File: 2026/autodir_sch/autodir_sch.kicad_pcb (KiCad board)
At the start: 2 copper layers, 34.5 x 16 mm, 12 parts, among them J1 UART, J2 MB, J3 PROG, U1 CH32V003JxMx, U2 ST485E

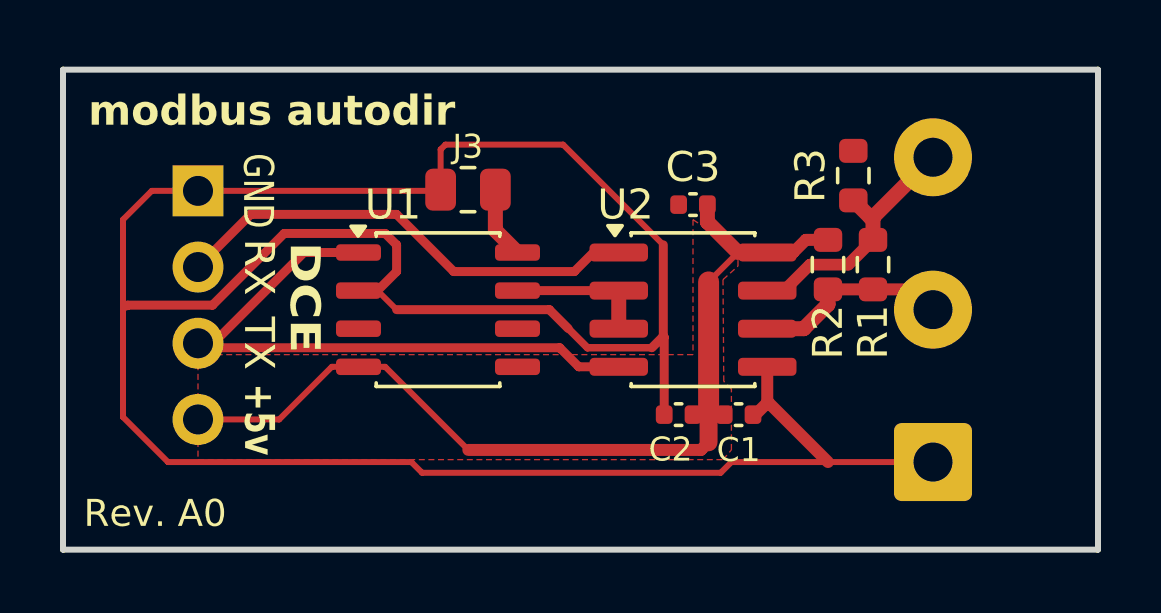
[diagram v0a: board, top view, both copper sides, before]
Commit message: RS485 automatic direction schematic and reference PCB
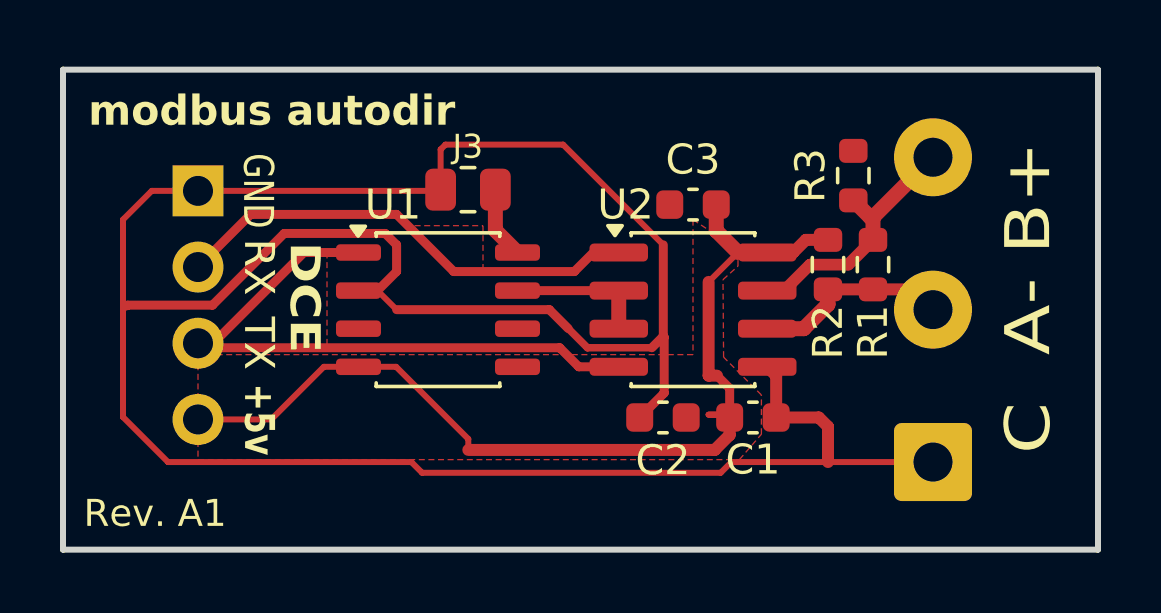
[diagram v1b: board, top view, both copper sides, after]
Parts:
- C1, C2, C3: footprint Capacitor_SMD:C_0402_1005Metric -> Capacitor_SMD:C_0603_1608Metric
- moved G*** 3.22 mm to (31.3, 18.2), turned to 45 degrees
- moved C2 0.53 mm to (38.5, 24.0)
- moved C1 0.49 mm to (41.5, 24.0)
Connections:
- net Net-(J2-Pin_2) renamed /A
- net Net-(J2-Pin_3) renamed /B
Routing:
- net GND: track 89.3 -> 90.6 mm
- net +5V: track 32.0 -> 33.1 mm
- added copper zone on F.Cu, net /DI
- added copper zone on F.Cu, net /RO
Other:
- board text added: "B+ A- C"
- board text added: "C A- B+"
